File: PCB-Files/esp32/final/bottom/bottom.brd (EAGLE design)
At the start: 50 x 31 mm, 41 parts, among them X2 ESP32_WROOM32_SKINNY

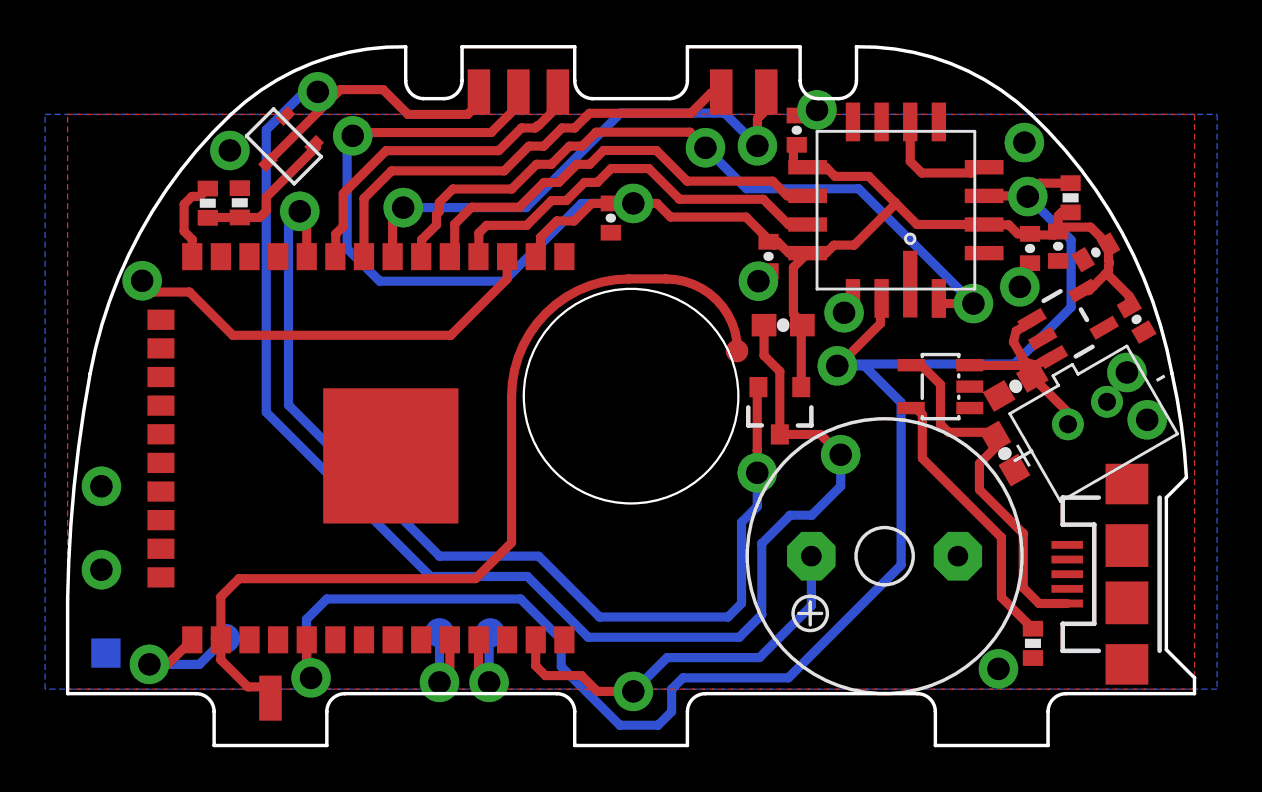
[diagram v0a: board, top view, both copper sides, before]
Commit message: creates final PCB version; revised beta side pcbs to match beta main pcb pinouts
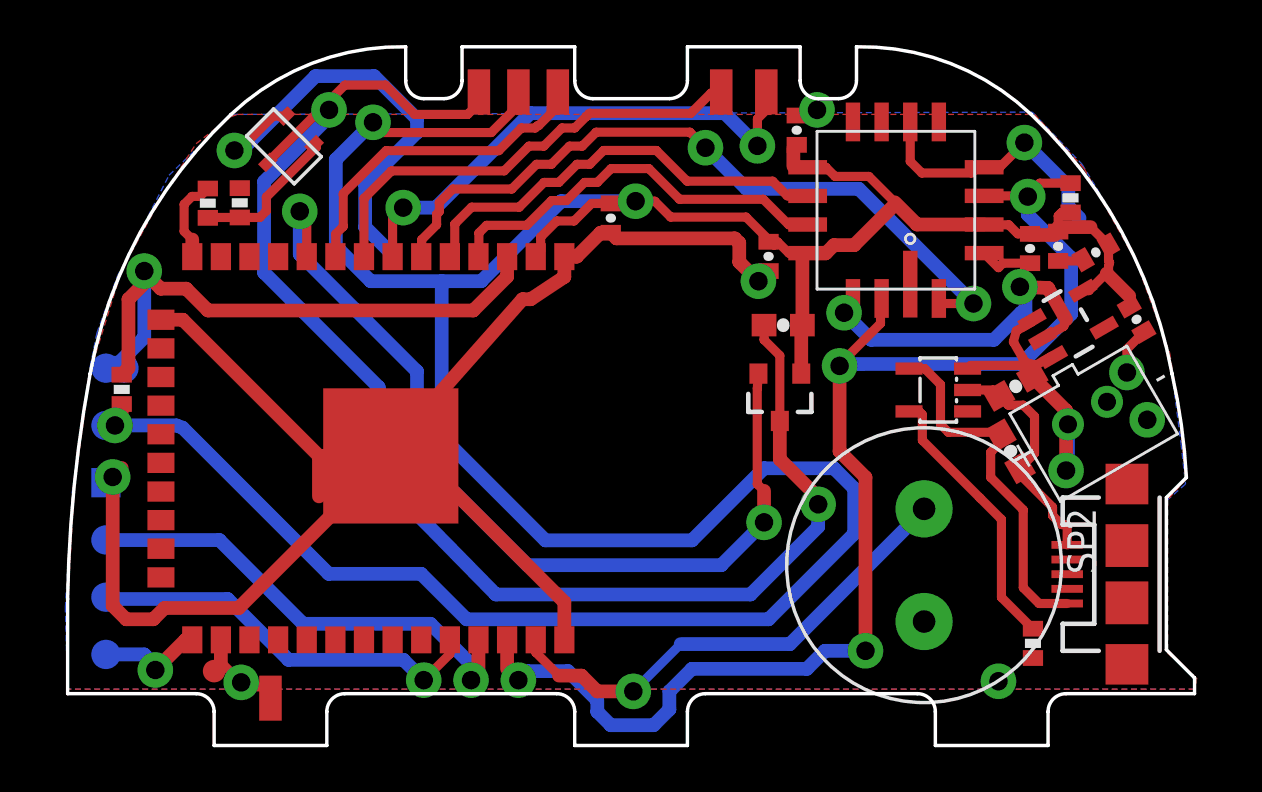
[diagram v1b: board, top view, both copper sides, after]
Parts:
- removed SP1: KSS1201, buzzer:KSS1201
- added R2: 10k, SparkFun-Passives:0402-RES
- added RESET1, RESET2: TPTP13R, testpad:TP13R
- added SP2: PS1240P02BT, adafruit:PS12
- R22: value 2k -> 4.7k
- moved CAP_MAGNET 27.2 mm to (6.50, 1.80)
- moved TX 17.5 mm to (1.70, 7.62)
- moved RX 14.9 mm to (1.70, 5.08)
- moved GND 7.56 mm to (1.70, 10.2)
- moved GPIO0 5.35 mm to (1.70, 2.54)
- moved RESET 4.09 mm to (1.70, 15.2)
- moved HALL 0.60 mm to (31.6, 14.0)
- moved C1 0.27 mm to (41.8, 11.6)
- moved CHARGER 0.18 mm to (38.6, 14.3)
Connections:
- removed net SCL: X2.36
- new net N$3: X2.29
- net ACCEL_SLEEP: now also X2.36; no longer X2.29
- net GND: now also SP2.P$2; no longer SP1.-
- net RESET: now also R2.1, RESET1.TP
- net SPEAKER: now also SP2.P$1; no longer SP1.+
- net VCC: now also R2.2, RESET2.TP
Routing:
- net GND: track 5.35 -> 136.8 mm, vias 11 -> 10
- net VCC: track 77.2 -> 147.7 mm, vias 2 -> 3
- net TOUCH: track 40.4 -> 5.17 mm, vias 0 -> 1
- net TX: track 4.30 -> 21.1 mm
- net RX: track 4.28 -> 18.4 mm
- net ACCEL_SLEEP: track 73.6 -> 60.0 mm, vias 3 -> 4
- net RESET: track 19.4 -> 28.7 mm
- net HALL_GND: track 72.6 -> 65.3 mm
- net HALL_4: track 45.1 -> 40.1 mm
- net SPEAKER: track 17.6 -> 21.9 mm
- net VBATT: track 10.0 -> 14.3 mm, vias 0 -> 1
- net GPIO0: track 6.20 -> 4.79 mm
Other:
- outline, holes or cut-outs redrawn
- board text added: "RESET Vcc GND Tx Rx GPIO0"
